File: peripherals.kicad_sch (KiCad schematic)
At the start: 49 parts, among them J15 Molex_PicoBlade_1x4_0533980471, J16 JST_SH_1x4_SM04B-SRSS-TB-LF-SN, J17 JST_SH_1x4_SM04B-SRSS-TB-LF-SN, Q13 PJE138K, Q14 PJE138K, U14 SLB9673AU20FW2610XTMA1, U51 NTS0102_XSON, U53 AP22653_DFN, U54 M24C64-F_DFN8, U55 AP22653_DFN

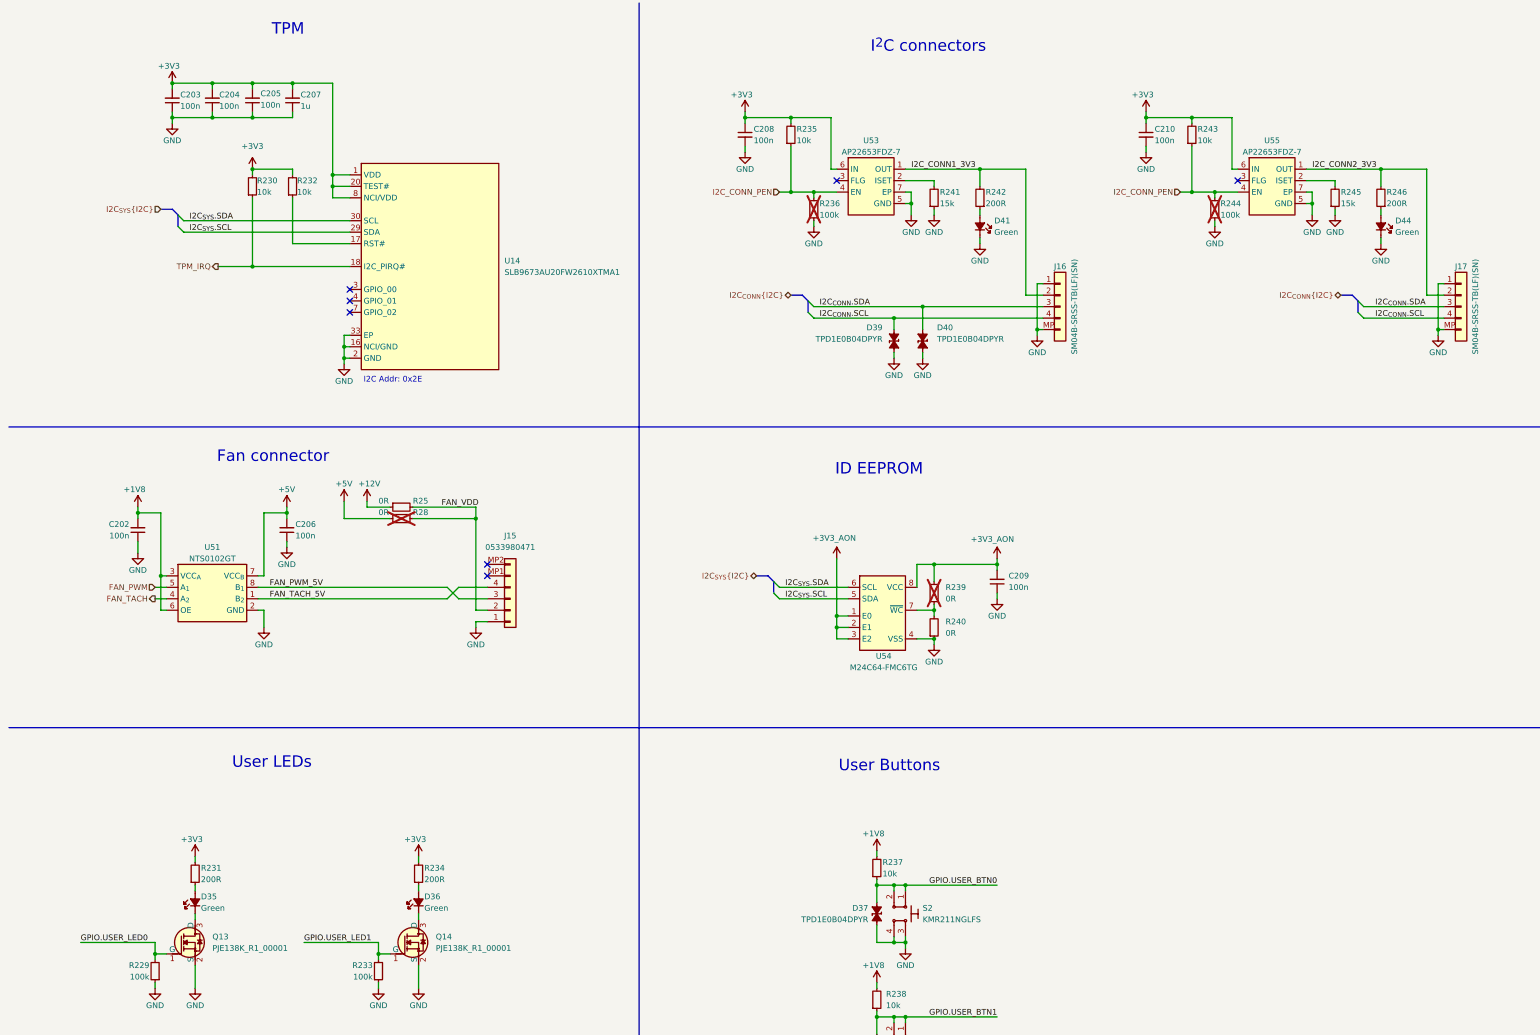
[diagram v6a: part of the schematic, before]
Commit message: [#85326] Add reviewers suggestions; Unify BOM
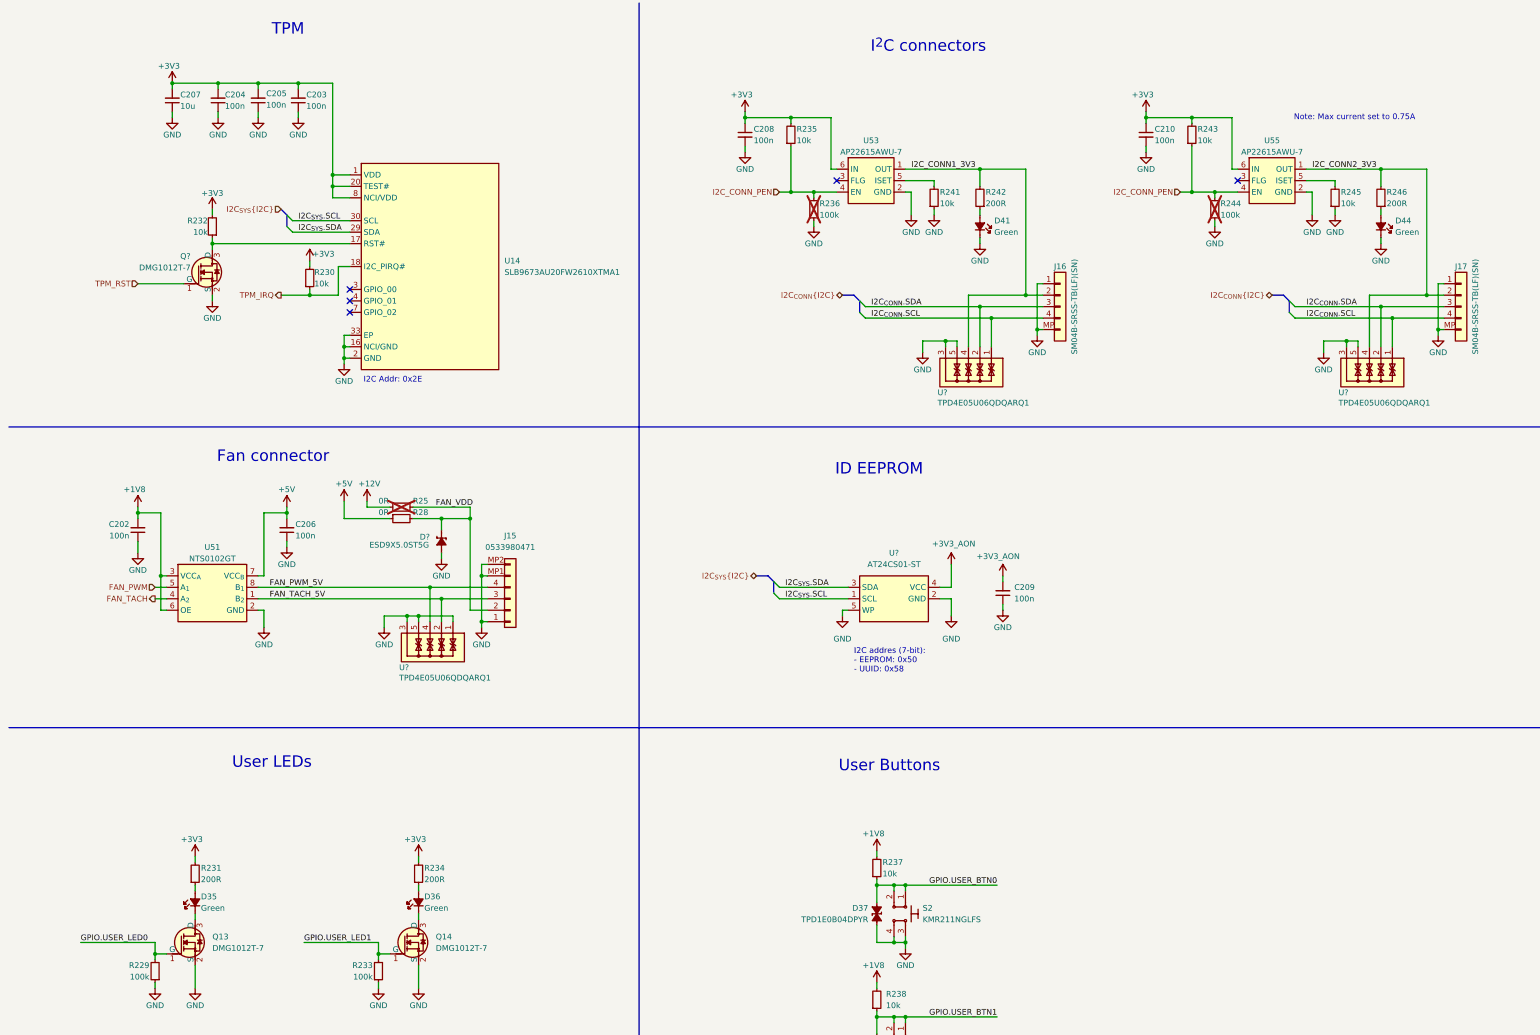
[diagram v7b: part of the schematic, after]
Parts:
- removed D39, D40: TPD1E0B04_XDFN-2, antmicro-footprints:XDFN-2_1x0.60mm, symbol antmicroTVSDiodes:TPD1E0B04_XDFN-2
- removed R239, R240: R_0R_0402, antmicro-footprints:R_0402_1005Metric, symbol antmicroResistors0402:R_0R_0402
- removed U54: M24C64-F_DFN8, antmicro-footprints:DFN-8-1EP_3x2mm_P0.5mm_EP1.36x1.46mm, symbol antmicroMemory:M24C64-F_DFN8
- added D?: ESD9X5.0ST5G, antmicro-footprints:SOD-923, symbol antmicroTVSDiodes:ESD9X5.0ST5G
- added Q?: DMG1012T-7, antmicro-footprints:SOT-523, symbol antmicroTransistorsFETsMOSFETsSingle:DMG1012T-7
- added U? (x3): TPD4E05U06QDQARQ1, antmicro-footprints:USON-10_2.5x1mm_P0.5mm, symbol antmicroTVSDiodes:TPD4E05U06QDQARQ1
- added U?: AT24CS01_SOT23, antmicro-footprints:SOT-23-5, symbol antmicroMemory:AT24CS01_SOT23
- C203, C204, C205: value C_100n_16V_X7R_0402 -> C_100n_0402; symbol antmicroCapacitors0402:C_100n_16V_X7R_0402 -> antmicroCapacitors0402:C_100n_0402; Dielectric X7R -> X5R; MPN C0402C104J4RAC7411 -> GRM155R61H104KE14D; Manufacturer KEMET -> Murata; Voltage 16V -> 50V
- C207: value C_1u_16V_0402 -> C_10u_0402; symbol antmicroCapacitors0402:C_1u_16V_0402 -> antmicroCapacitors0402:C_10u_0402; MPN C0402C105M4PACTU -> CC0402MRX5R5BB106; Manufacturer KEMET -> YAGEO; Val 1u -> 10u
- Q13, Q14: value PJE138K -> DMG1012T-7; symbol antmicroTransistorsFETsMOSFETsSingle:PJE138K -> antmicroTransistorsFETsMOSFETsSingle:DMG1012T-7; MPN PJE138K_R1_00001 -> DMG1012T-7; Manufacturer PANJIT -> Diodes Incorporated
- R241, R245: value R_15k_0402 -> R_10k_0402; symbol antmicroResistors0402:R_15k_0402 -> antmicroResistors0402:R_10k_0402; MPN CR0402-FX-1502GLF -> CR0402-FX-1002GLF; Val 15k -> 10k
- R25: now not fitted; now left out of the parts list
- R28: now fitted
- U53, U55: value AP22653_DFN -> AP22615A_TSOT26; footprint antmicro-footprints:DFN-6-1EP_2x2mm_P0.65mm_EP1x1.6mm -> antmicro-footprints:TSOT23-6; symbol antmicroPMICPowerDistributionSwitchesLoadDrivers:AP22653_DFN -> antmicroPMICPowerDistributionSwitchesLoadDrivers:AP22615A_TSOT26; MPN AP22653FDZ-7 -> AP22615AWU-7
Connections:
- net +3V3_AON: now also U?.4 (VCC)
- net FAN_PWM_5V: now also J15.4, U?.4, U?.7; no longer J15.3
- net FAN_TACH_5V: now also J15.3, U?.2, U?.9; no longer J15.4
- net FAN_VDD: now also D?.1 (C)
- net GND: now also J15.MP1, J15.MP2, U53.2 (GND), U55.2 (GND), D?.2 (A), Q?.2 (S), U?.1, U?.10, U?.2 (GND), U?.3, U?.3, U?.3, U?.5, U?.5, U?.5, U?.5 (WP), U?.6, U?.6, U?.6, U?.8, U?.8, U?.8; no longer U53.5 (GND), U53.7 (EP), U55.5 (GND), U55.7 (EP)
- net I2C_CONN1_3V3: now also U?.4, U?.7
- net I2C_CONN2_3V3: now also U?.4, U?.7
- net I2C_{CONN}.SCL: now also U?.1, U?.1, U?.10, U?.10
- net I2C_{CONN}.SDA: now also U?.2, U?.2, U?.9, U?.9
- net I2C_{SYS}.SCL: now also U14.30 (SCL), U?.1 (SCL); no longer U14.29 (SDA)
- net I2C_{SYS}.SDA: now also U14.29 (SDA), U?.3 (SDA); no longer U14.30 (SCL)
- net at R245.2: now also U55.5 (ISET); no longer U55.2 (ISET)
- net at R232.1, U14.17 (RST#): now also Q?.3 (D)
- net at R241.2: now also U53.5 (ISET); no longer U53.2 (ISET)
- new net TPM_RST: Q?.1 (G)
- no-connect marks 7 -> 5
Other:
- note added: "I2C addres (7-bit): - EEPROM: 0x50 - UUID: 0x58"
- note added: "Note: Max current set to 0.75A"
- moved on the sheet: C203, C204, C205, C207, C209, R230, R232

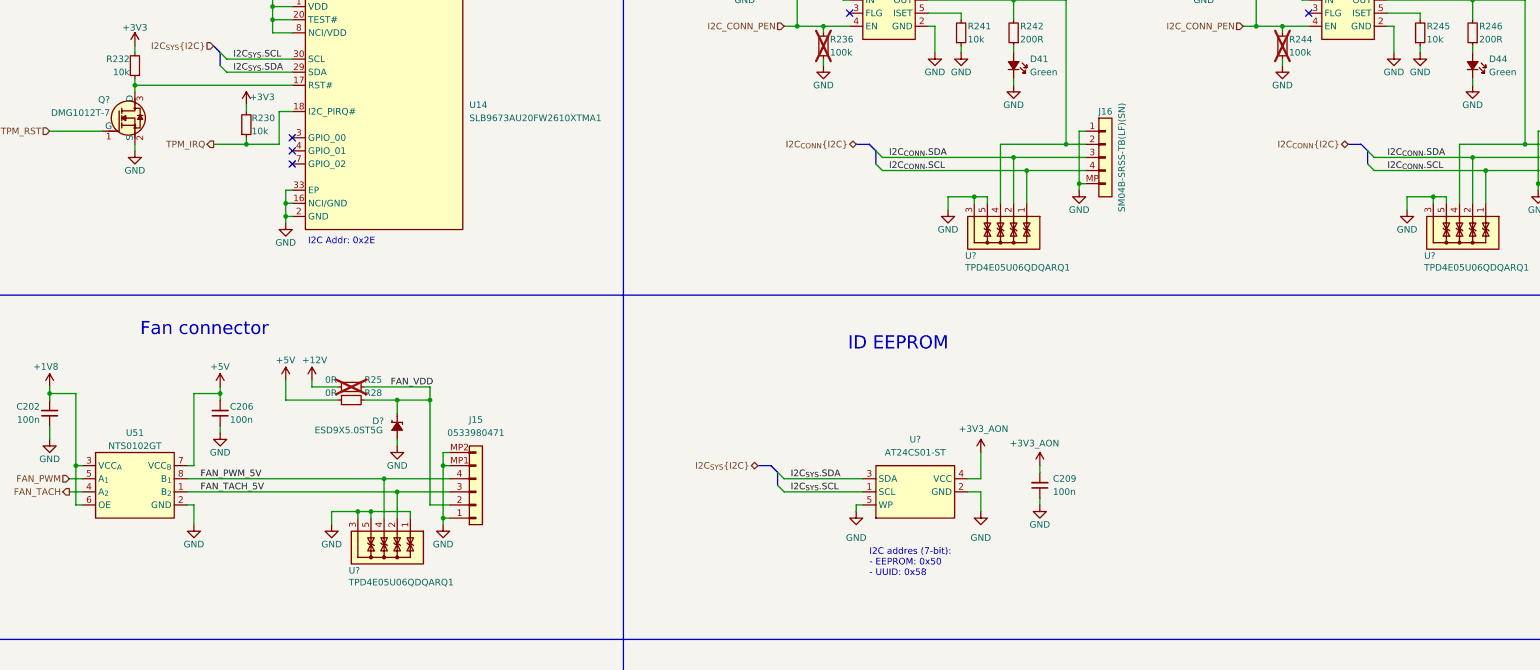
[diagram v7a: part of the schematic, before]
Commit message: [#85326] Fix annotation, set USBPD ideal diodes to DNP, add DC-DC rule zones
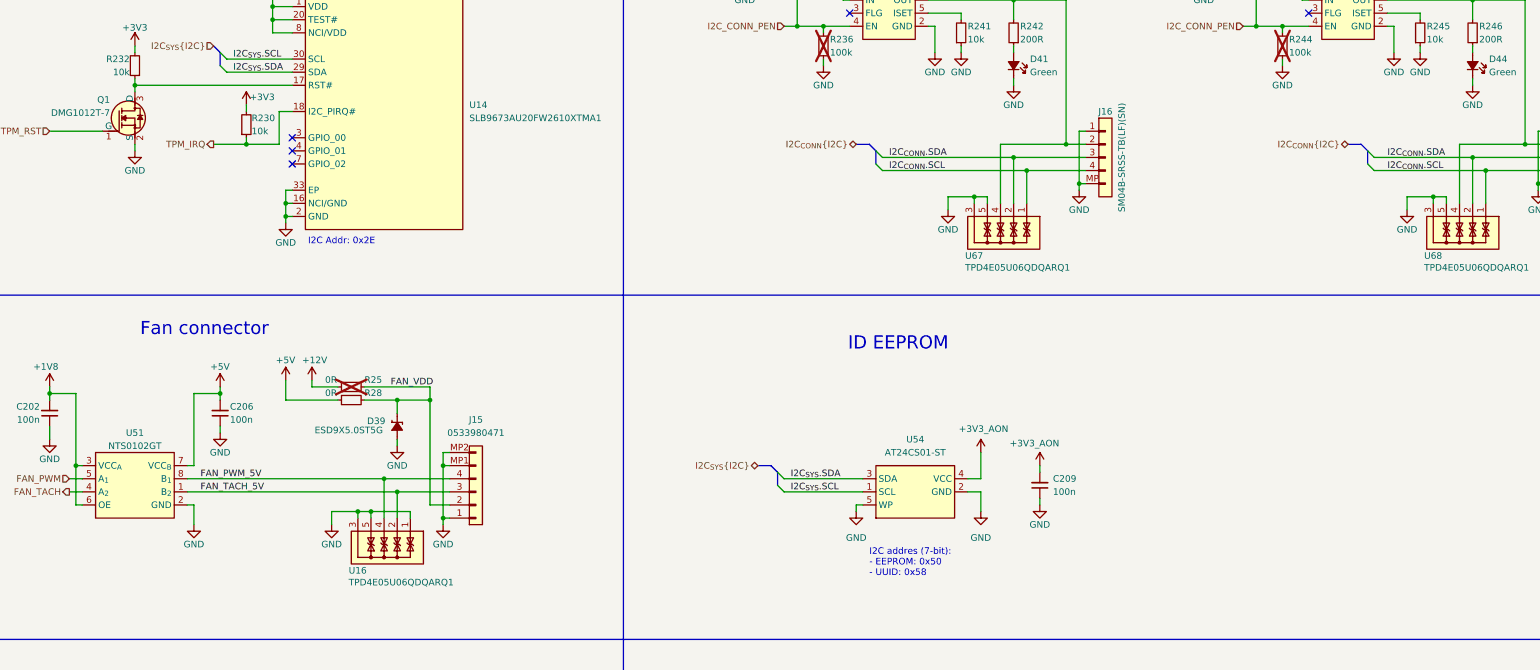
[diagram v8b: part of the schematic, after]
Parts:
- removed D?: ESD9X5.0ST5G, antmicro-footprints:SOD-923, symbol antmicroTVSDiodes:ESD9X5.0ST5G
- removed Q?: DMG1012T-7, antmicro-footprints:SOT-523, symbol antmicroTransistorsFETsMOSFETsSingle:DMG1012T-7
- removed U? (x3): TPD4E05U06QDQARQ1, antmicro-footprints:USON-10_2.5x1mm_P0.5mm, symbol antmicroTVSDiodes:TPD4E05U06QDQARQ1
- added D39: ESD9X5.0ST5G, antmicro-footprints:SOD-923, symbol antmicroTVSDiodes:ESD9X5.0ST5G
- added Q1: DMG1012T-7, antmicro-footprints:SOT-523, symbol antmicroTransistorsFETsMOSFETsSingle:DMG1012T-7
- added U16, U67, U68: TPD4E05U06QDQARQ1, antmicro-footprints:USON-10_2.5x1mm_P0.5mm, symbol antmicroTVSDiodes:TPD4E05U06QDQARQ1
- gave numbers to parts that had none: 1
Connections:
- net FAN_PWM_5V: now also U16.4, U16.7
- net FAN_TACH_5V: now also U16.2, U16.9
- net FAN_VDD: now also D39.1 (C)
- net GND: now also D39.2 (A), Q1.2 (S), U16.1, U16.10, U16.3, U16.5, U16.6, U16.8, U67.3, U67.5, U67.6, U67.8, U68.3, U68.5, U68.6, U68.8
- net I2C_CONN1_3V3: now also U67.4, U67.7
- net I2C_CONN2_3V3: now also U68.4, U68.7
- net I2C_{CONN}.SCL: now also U67.1, U67.10, U68.1, U68.10
- net I2C_{CONN}.SDA: now also U67.2, U67.9, U68.2, U68.9
- net TPM_RST: now also Q1.1 (G)
- net at R232.1, U14.17 (RST#): now also Q1.3 (D)
